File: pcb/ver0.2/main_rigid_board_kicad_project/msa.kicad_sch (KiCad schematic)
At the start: 50 parts, among them J2 SWD Prog, U1 MCP1702, U2 MCP73831-2-OT, U3 W25Q128JV, U4 RP2040, Y1 H130B-12.000-20-3050-EXT-TR

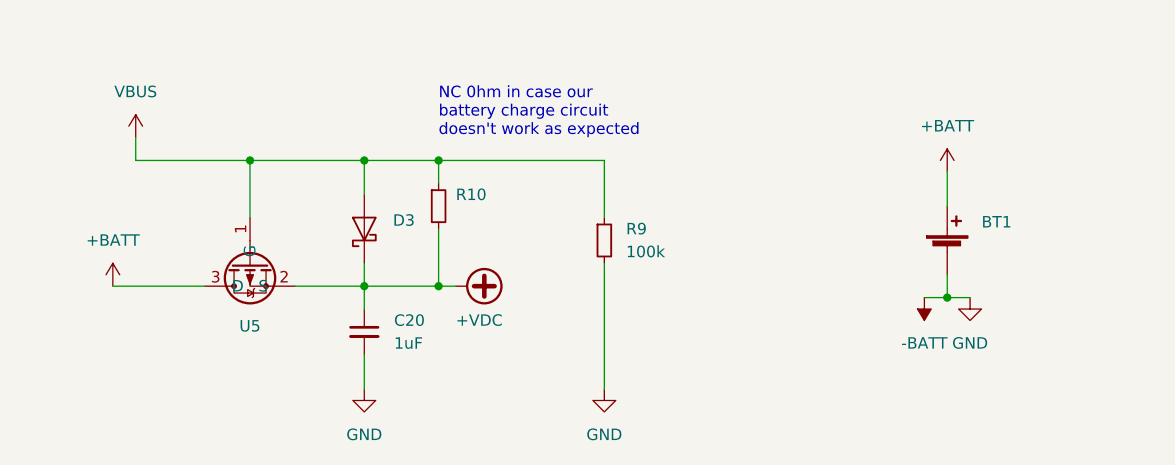
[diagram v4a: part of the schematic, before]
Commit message: change usb to proper right angle, set 45 mm spacing of microphones and proper overhang space
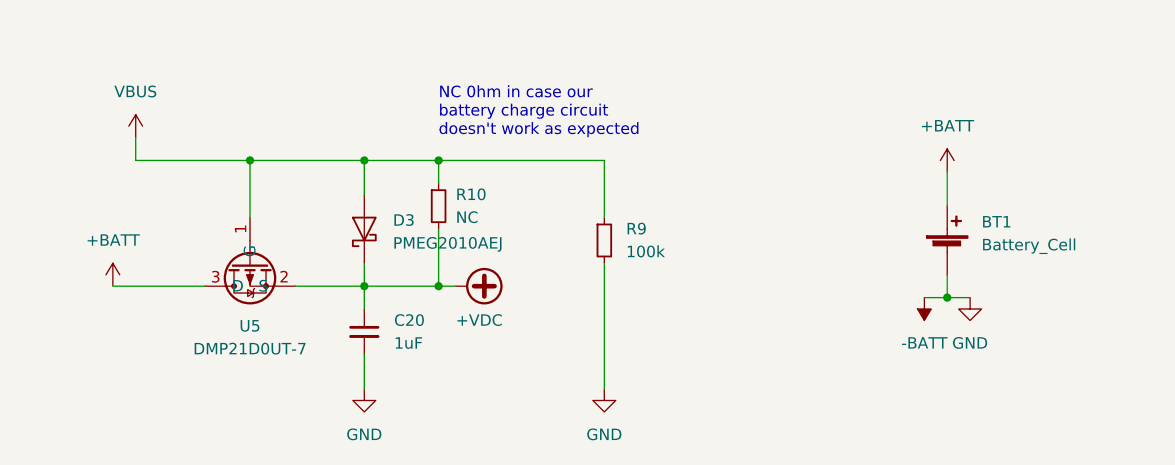
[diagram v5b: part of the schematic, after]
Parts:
- BT1: value (none) -> Battery_Cell; footprint (none) -> OpenSourceSmartGlasses:BatterySolderOn
- D3: value (none) -> PMEG2010AEJ; footprint (none) -> Diode_SMD:D_SOD-323F
- R10: value (none) -> NC; footprint (none) -> Resistor_SMD:R_0402_1005Metric
- U5: value (none) -> ‎DMP21D0UT-7‎
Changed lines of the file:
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@@
       (effects (font (size 1.27 1.27)) (justify left))
     )
-    (property "Value" "" (id 1) (at 416.56 185.9279 0)
-      (effects (font (size 1.27 1.27)) (justify left))
-    )
-    (property "Footprint" "" (id 2) (at 412.75 185.166 90)
+    (property "Value" "Battery_Cell" (id 1) (at 416.56 185.9279 0)
+      (effects (font (size 1.27 1.27)) (justify left))
+    )
+    (property "Footprint" "OpenSourceSmartGlasses:BatterySolderOn" (id 2) (at 412.75 185.166 90)
       (effects (font (size 1.27 1.27)) hide)
     )
@@
     (in_bom yes) (on_board yes) (fields_autoplaced)
     (property "Reference" "U5" (id 0) (at 335.28 194.945 90))
-    (property "Value" "" (id 1) (at 335.28 197.485 90))
+    (property "Value" "‎DMP21D0UT-7‎" (id 1) (at 335.28 197.485 90))
     (property "Footprint" "Package_TO_SOT_SMD:SOT-523" (id 2) (at 335.28 190.5 0)
       (effects (font (size 1.27 1.27)) hide)
@@
       (effects (font (size 1.27 1.27)) (justify right))
     )
-    (property "Value" "" (id 1) (at 351.155 185.7374 90)
+    (property "Value" "PMEG2010AEJ" (id 1) (at 351.155 185.7374 90)
       (effects (font (size 1.27 1.27)) (justify right))
     )
-    (property "Footprint" "" (id 2) (at 352.425 184.15 0)
+    (property "Footprint" "Diode_SMD:D_SOD-323F" (id 2) (at 352.425 184.15 0)
       (effects (font (size 1.27 1.27)) hide)
     )
@@
   )
   (symbol (lib_id "Connector:USB_B_Micro") (at 30.48 33.02 0) (unit 1)
-    (in_bom yes) (on_board yes) (fields_autoplaced)
+    (in_bom yes) (on_board yes)
     (property "Reference" "J1" (id 0) (at 30.48 19.685 0))
     (property "Value" "" (id 1) (at 30.48 22.225 0))
-    (property "Footprint" "" (id 2) (at 34.29 34.29 0))
+    (property "Footprint" "" (id 2) (at 34.29 34.29 0)
+      (effects (font (size 1.27 1.27)) hide)
+    )
     (property "Datasheet" "~" (id 3) (at 34.29 34.29 0)
       (effects (font (size 1.27 1.27)) hide)
@@
       (effects (font (size 1.27 1.27)) (justify left))
     )
-    (property "Value" "" (id 1) (at 358.14 182.8799 0)
-      (effects (font (size 1.27 1.27)) (justify left))
-    )
-    (property "Footprint" "" (id 2) (at 356.235 181.61 0)
+    (property "Value" "NC" (id 1) (at 358.14 182.8799 0)
+      (effects (font (size 1.27 1.27)) (justify left))
+    )
+    (property "Footprint" "Resistor_SMD:R_0402_1005Metric" (id 2) (at 356.235 181.61 0)
       (effects (font (size 1.27 1.27)) hide)
     )
@@
     )
     (path "/ced7dc34-db35-4899-ac7f-ee11e1970548"
-      (reference "J1") (unit 1) (value "USB_B_Micro") (footprint "Connector_USB:USB_Micro-B_Molex-105133-0001")
+      (reference "J1") (unit 1) (value "USB_B_Micro") (footprint "OpenSourceSmartGlasses:micro_usb_right_angle_1050170001_molex")
     )
     (path "/00000000-0000-0000-0000-000061bb7e1f"

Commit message: latest working mic array
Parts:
- added H1, H2: MountingHole, OpenSourceSmartGlasses:Mount_hole_small_0.7mm, symbol Mechanical:MountingHole
- added SW1: SW_SPST, Button_Switch_SMD:SW_SPST_B3U-3100P-B, symbol Switch:SW_SPST
- CONN1: value slim_stack_receptable_12pos_5035481222_schematic -> (none); footprint OpenSourceSmartGlasses:slim_stack_molex_PLUG_5035521222 -> (none)
- D2: footprint Capacitor_SMD:C_0402_1005Metric_Pad0.74x0.62mm_HandSolder -> LED_SMD:LED_0402_1005Metric
- J1: value (none) -> USB_B_Micro; footprint (none) -> OpenSourceSmartGlasses:micro_usb_right_angle_1050170001_molex
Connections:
- net +3V3: now also CONN1.1; no longer CONN1.6
- net -BATT: now also CONN1.8, R6.1, SW1.2 (B); no longer CONN1.11, D1.1 (K)
- net MIC_CLK: now also CONN1.2; no longer CONN1.5
- net MIC_DOUT_0: now also CONN1.12; no longer CONN1.7
- net MIC_DOUT_1: now also CONN1.11; no longer CONN1.8
- net MIC_DOUT_2: now also CONN1.10; no longer CONN1.9
- net MIC_DOUT_3: now also CONN1.9; no longer CONN1.10
- net RED_LED: now also D1.2 (A); no longer R6.2
- net USB_BOOT: now also SW1.1 (A)
- new net: D1.1 (K), R6.2
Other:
- moved on the sheet: D1, R6
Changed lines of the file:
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@@
   (junction (at 212.09 36.83) (diameter 0) (color 0 0 0 0)
   )
+  (junction (at 30.48 168.91) (diameter 0) (color 0 0 0 0)
+  )
   (junction (at 347.98 190.5) (diameter 0) (color 0 0 0 0)
   )
@@
   )
   (junction (at 132.08 48.26) (diameter 0) (color 0 0 0 0)
+  )
+  (junction (at 21.59 183.515) (diameter 0) (color 0 0 0 0)
   )
   (junction (at 266.7 182.88) (diameter 0) (color 0 0 0 0)
@@
     (stroke (width 0) (type default) (color 0 0 0 0))
   )
+  (wire (pts (xy 21.59 183.515) (xy 30.48 183.515))
+    (stroke (width 0) (type default) (color 0 0 0 0))
+  )
   (wire (pts (xy 57.15 71.12) (xy 59.69 71.12))
     (stroke (width 0) (type default) (color 0 0 0 0))
@@
     (stroke (width 0) (type default) (color 0 0 0 0))
   )
+  (wire (pts (xy 30.48 182.245) (xy 30.48 183.515))
+    (stroke (width 0) (type default) (color 0 0 0 0))
+  )
   (wire (pts (xy 193.04 44.45) (xy 193.04 46.99))
     (stroke (width 0) (type default) (color 0 0 0 0))
@@
     (stroke (width 0) (type default) (color 0 0 0 0))
   )
-  (wire (pts (xy 33.02 168.91) (xy 21.59 168.91))
+  (wire (pts (xy 33.02 168.91) (xy 30.48 168.91))
     (stroke (width 0) (type default) (color 0 0 0 0))
   )
@@
     (stroke (width 0) (type default) (color 0 0 0 0))
   )
+  (wire (pts (xy 21.59 183.515) (xy 21.59 184.15))
+    (stroke (width 0) (type default) (color 0 0 0 0))
+  )
   (wire (pts (xy 267.97 39.37) (xy 273.05 39.37))
     (stroke (width 0) (type default) (color 0 0 0 0))
@@
     (stroke (width 0) (type default) (color 0 0 0 0))
   )
+  (wire (pts (xy 30.48 168.91) (xy 21.59 168.91))
+    (stroke (width 0) (type default) (color 0 0 0 0))
+  )
   (wire (pts (xy 182.88 138.43) (xy 193.04 138.43))
     (stroke (width 0) (type default) (color 0 0 0 0))
@@
     (stroke (width 0) (type default) (color 0 0 0 0))
   )
-  (wire (pts (xy 21.59 181.61) (xy 21.59 184.15))
+  (wire (pts (xy 21.59 181.61) (xy 21.59 183.515))
     (stroke (width 0) (type default) (color 0 0 0 0))
   )
@@
   )
   (wire (pts (xy 27.94 45.72) (xy 30.48 45.72))
+    (stroke (width 0) (type default) (color 0 0 0 0))
+  )
+  (wire (pts (xy 30.48 168.91) (xy 30.48 172.085))
     (stroke (width 0) (type default) (color 0 0 0 0))
   )
@@
     (pin "2")
   )
-  (symbol (lib_id "Device:R_Small") (at 255.27 39.37 270) (unit 1)
-    (in_bom yes) (on_board yes)
-    (property "Reference" "R6" (id 0) (at 254 34.29 90)
-      (effects (font (size 1.27 1.27)) (justify left))
-    )
-    (property "Value" "470R" (id 1) (at 254 36.83 90)
-      (effects (font (size 1.27 1.27)) (justify left))
-    )
-    (property "Footprint" "Resistor_SMD:R_0402_1005Metric" (id 2) (at 255.27 39.37 0)
-      (effects (font (size 1.27 1.27)) hide)
-    )
-    (property "Datasheet" "~" (id 3) (at 255.27 39.37 0)
-      (effects (font (size 1.27 1.27)) hide)
-    )
-    (pin "1")
-    (pin "2")
-  )
-  (symbol (lib_id "Device:LED_Small") (at 265.43 39.37 180) (unit 1)
-    (in_bom yes) (on_board yes)
-    (property "Reference" "D1" (id 0) (at 265.43 34.1122 0))
-    (property "Value" "APA3010SECK" (id 1) (at 265.43 36.4236 0))
-    (property "Footprint" "LED_SMD:LED_0402_1005Metric" (id 2) (at 265.43 39.37 90)
-      (effects (font (size 1.27 1.27)) hide)
-    )
-    (property "Datasheet" "~" (id 3) (at 265.43 39.37 90)
+  (symbol (lib_id "Device:R_Small") (at 265.43 39.37 270) (unit 1)
+    (in_bom yes) (on_board yes)
+    (property "Reference" "R6" (id 0) (at 264.16 34.29 90)
+      (effects (font (size 1.27 1.27)) (justify left))
+    )
+    (property "Value" "470R" (id 1) (at 264.16 36.83 90)
+      (effects (font (size 1.27 1.27)) (justify left))
+    )
+    (property "Footprint" "Resistor_SMD:R_0402_1005Metric" (id 2) (at 265.43 39.37 0)
+      (effects (font (size 1.27 1.27)) hide)
+    )
+    (property "Datasheet" "~" (id 3) (at 265.43 39.37 0)
+      (effects (font (size 1.27 1.27)) hide)
+    )
+    (pin "1")
+    (pin "2")
+  )
+  (symbol (lib_id "Device:LED_Small") (at 255.27 39.37 180) (unit 1)
+    (in_bom yes) (on_board yes)
+    (property "Reference" "D1" (id 0) (at 255.27 34.1122 0))
+    (property "Value" "APA3010SECK" (id 1) (at 255.27 36.4236 0))
+    (property "Footprint" "LED_SMD:LED_0402_1005Metric" (id 2) (at 255.27 39.37 90)
+      (effects (font (size 1.27 1.27)) hide)
+    )
+    (property "Datasheet" "~" (id 3) (at 255.27 39.37 90)
       (effects (font (size 1.27 1.27)) hide)
     )
@@
       (effects (font (size 1.27 1.27)) (justify left))
     )
-    (property "Footprint" "Capacitor_SMD:C_0402_1005Metric_Pad0.74x0.62mm_HandSolder" (id 2) (at 250.19 180.34 0)
+    (property "Footprint" "LED_SMD:LED_0402_1005Metric" (id 2) (at 250.19 180.34 0)
       (effects (font (size 1.27 1.27)) hide)
     )
@@
       (effects (font (size 1.27 1.27)) (justify left))
     )
-    (property "Value" "slim_stack_receptable_12pos_5035481222_schematic" (id 1) (at 67.31 111.7599 0)
-      (effects (font (size 1.27 1.27)) (justify left))
-    )
-    (property "Footprint" "OpenSourceSmartGlasses:slim_stack_molex_PLUG_5035521222" (id 2) (at 45.72 92.71 0)
+    (property "Value" "" (id 1) (at 67.31 111.7599 0)
+      (effects (font (size 1.27 1.27)) (justify left))
+    )
+    (property "Footprint" "" (id 2) (at 45.72 92.71 0)
       (effects (font (size 1.27 1.27)) hide)
     )
@@
     (pin "9")
   )
+  (symbol (lib_id "Mechanical:MountingHole") (at 349.25 36.195 0) (unit 1)
+    (in_bom yes) (on_board yes) (fields_autoplaced)
+    (property "Reference" "H2" (id 0) (at 352.425 34.9249 0)
+      (effects (font (size 1.27 1.27)) (justify left))
+    )
+    (property "Value" "MountingHole" (id 1) (at 352.425 37.4649 0)
+      (effects (font (size 1.27 1.27)) (justify left))
+    )
+    (property "Footprint" "OpenSourceSmartGlasses:Mount_hole_small_0.7mm" (id 2) (at 349.25 36.195 0)
+      (effects (font (size 1.27 1.27)) hide)
+    )
+    (property "Datasheet" "~" (id 3) (at 349.25 36.195 0)
+      (effects (font (size 1.27 1.27)) hide)
+    )
+  )
   (symbol (lib_id "power:-BATT") (at 410.21 191.77 180) (unit 1)
     (in_bom yes) (on_board yes) (fields_autoplaced)
@@
     )
     (pin "1")
+  )
+  (symbol (lib_id "Mechanical:MountingHole") (at 327.025 36.83 0) (unit 1)
+    (in_bom yes) (on_board yes) (fields_autoplaced)
+    (property "Reference" "H1" (id 0) (at 330.2 35.5599 0)
+      (effects (font (size 1.27 1.27)) (justify left))
+    )
+    (property "Value" "MountingHole" (id 1) (at 330.2 38.0999 0)
+      (effects (font (size 1.27 1.27)) (justify left))
+    )
+    (property "Footprint" "OpenSourceSmartGlasses:Mount_hole_small_0.7mm" (id 2) (at 327.025 36.83 0)
+      (effects (font (size 1.27 1.27)) hide)
+    )
+    (property "Datasheet" "~" (id 3) (at 327.025 36.83 0)
+      (effects (font (size 1.27 1.27)) hide)
+    )
   )
   (symbol (lib_id "power:+BATT") (at 266.7 181.61 90) (unit 1)
@@
     )
     (property "Datasheet" "~" (id 3) (at 374.65 185.42 0)
+      (effects (font (size 1.27 1.27)) hide)
+    )
+    (pin "1")
+    (pin "2")
+  )
+  (symbol (lib_id "Switch:SW_SPST") (at 30.48 177.165 270) (unit 1)
+    (in_bom yes) (on_board yes) (fields_autoplaced)
+    (property "Reference" "SW1" (id 0) (at 33.02 175.8949 90)
+      (effects (font (size 1.27 1.27)) (justify left))
+    )
+    (property "Value" "SW_SPST" (id 1) (at 33.02 178.4349 90)
+      (effects (font (size 1.27 1.27)) (justify left))
+    )
+    (property "Footprint" "Button_Switch_SMD:SW_SPST_B3U-3100P-B" (id 2) (at 30.48 177.165 0)
+      (effects (font (size 1.27 1.27)) hide)
+    )
+    (property "Datasheet" "~" (id 3) (at 30.48 177.165 0)
       (effects (font (size 1.27 1.27)) hide)
     )
@@
     (in_bom yes) (on_board yes)
     (property "Reference" "J1" (id 0) (at 30.48 19.685 0))
-    (property "Value" "" (id 1) (at 30.48 22.225 0))
-    (property "Footprint" "" (id 2) (at 34.29 34.29 0)
+    (property "Value" "USB_B_Micro" (id 1) (at 30.48 22.225 0))
+    (property "Footprint" "OpenSourceSmartGlasses:micro_usb_right_angle_1050170001_molex" (id 2) (at 34.29 34.29 0)
       (effects (font (size 1.27 1.27)) hide)
     )
@@
     )
     (path "/2b3f38bb-dc91-41db-88d5-8b07790a4f71"
-      (reference "CONN1") (unit 1) (value "slim_stack_receptable_12pos_5035481222_schematic") (footprint "OpenSourceSmartGlasses:slim_stack_molex_PLUG_5035521222")
+      (reference "CONN1") (unit 1) (value "slim_stack_receptable_12pos_5035481222_schematic") (footprint "OpenSourceSmartGlasses:slim_stack_molex_RECEPTACLE_5035481222")
     )
     (path "/00000000-0000-0000-0000-000061b9072f"
@@
     )
     (path "/223083af-ea1a-4483-9ccd-9a44d99c1e56"
-      (reference "D2") (unit 1) (value "LED") (footprint "Capacitor_SMD:C_0402_1005Metric_Pad0.74x0.62mm_HandSolder")
+      (reference "D2") (unit 1) (value "LED") (footprint "LED_SMD:LED_0402_1005Metric")
     )
     (path "/5c9aa413-b666-48d1-891f-dbf31f3906c2"
       (reference "D3") (unit 1) (value "PMEG2010AEJ") (footprint "Diode_SMD:D_SOD-323F")
     )
+    (path "/59d7a021-9bba-4a8d-b927-56a85207d59e"
+      (reference "H1") (unit 1) (value "MountingHole") (footprint "OpenSourceSmartGlasses:Mount_hole_small_0.7mm")
+    )
+    (path "/3f9ba76a-e880-4988-91ed-4af51b2b79d6"
+      (reference "H2") (unit 1) (value "MountingHole") (footprint "OpenSourceSmartGlasses:Mount_hole_small_0.7mm")
+    )
     (path "/ced7dc34-db35-4899-ac7f-ee11e1970548"
       (reference "J1") (unit 1) (value "USB_B_Micro") (footprint "OpenSourceSmartGlasses:micro_usb_right_angle_1050170001_molex")
@@
       (reference "R10") (unit 1) (value "NC") (footprint "Resistor_SMD:R_0402_1005Metric")
     )
+    (path "/99bd7f69-e007-4523-a21b-a75557f73c96"
+      (reference "SW1") (unit 1) (value "SW_SPST") (footprint "Button_Switch_SMD:SW_SPST_B3U-3100P-B")
+    )
     (path "/00000000-0000-0000-0000-000061a37de0"
